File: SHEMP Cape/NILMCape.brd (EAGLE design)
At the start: 54.6 x 71.8 mm, 26 parts, among them U1 ADS8568_PM_64, U2 ACS756KCA-050B-PFF-T, U3 LTC6082, U4 LTC6082, U5 LM2687_DGK_8

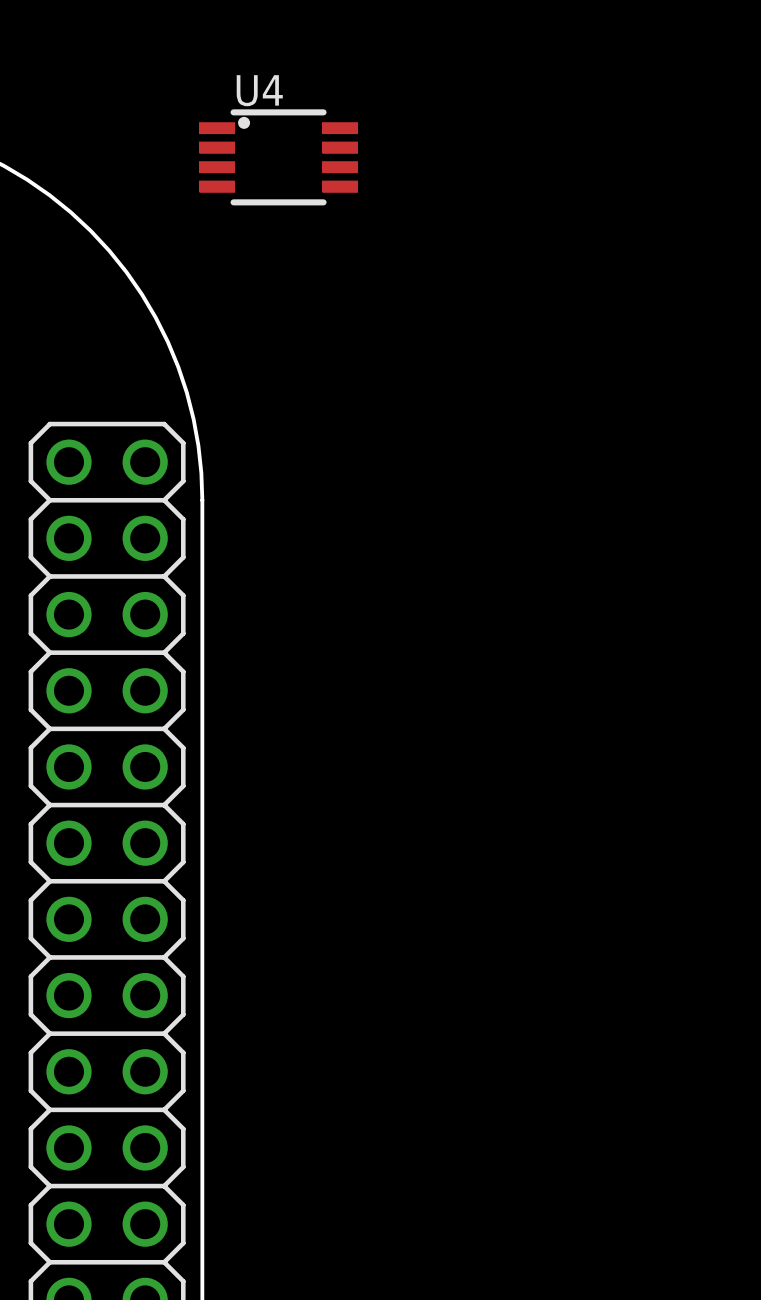
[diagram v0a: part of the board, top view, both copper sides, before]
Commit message: Added Frequency Response
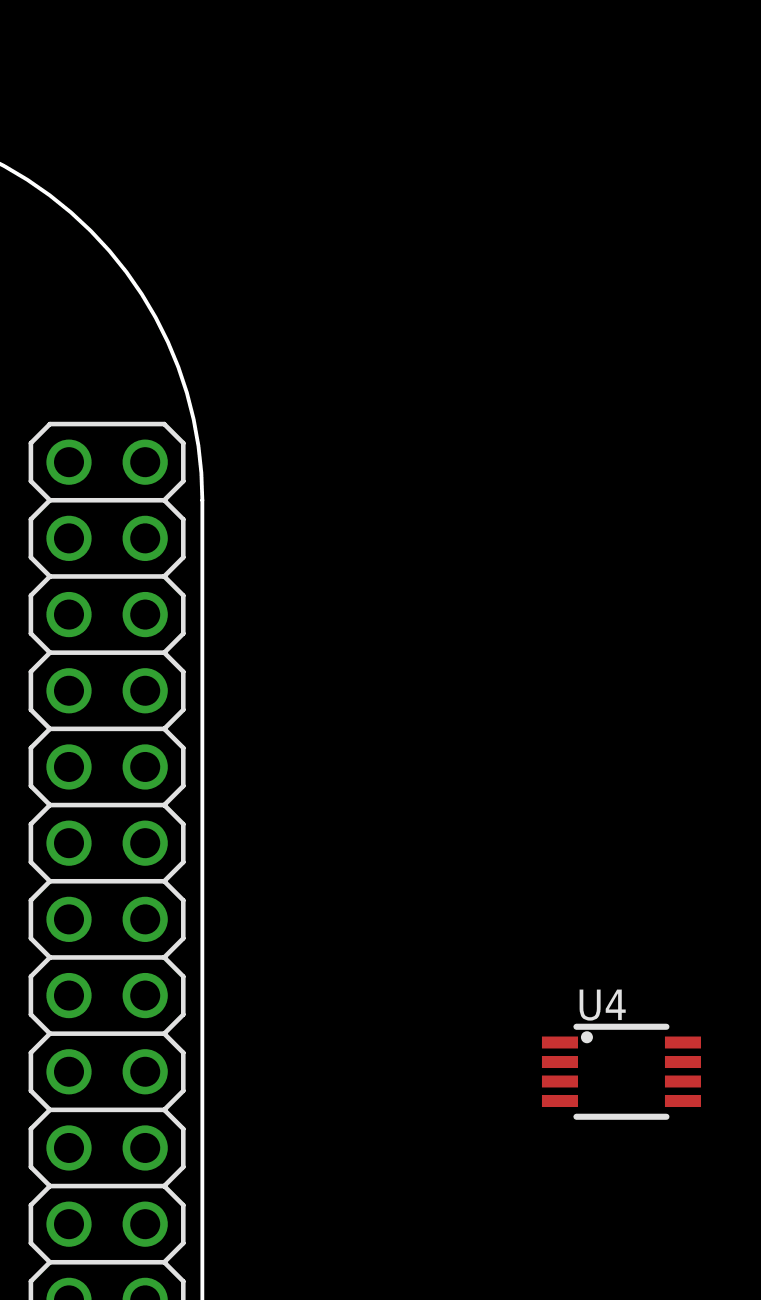
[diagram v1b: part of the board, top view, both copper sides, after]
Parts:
- moved U4 32.6 mm to (68.6, 54.6)
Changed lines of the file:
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@@
 <?xml version="1.0" encoding="utf-8"?>
 <!DOCTYPE eagle SYSTEM "eagle.dtd">
-<eagle version="6.4">
+<eagle version="6.5.0">
 <drawing>
 <settings>
@@
 <attribute name="VALUE" x="19.97" y="87.71" size="1.27" layer="27" font="vector"/>
 </element>
-<element name="U4" library="SensorCape" package="MSOP8" value="LTC6082" x="57.15" y="85.09" smashed="yes" rot="R270">
-<attribute name="NAME" x="55.646" y="86.814" size="1.016" layer="25"/>
-<attribute name="VALUE" x="55.538" y="82.262" size="1.016" layer="27"/>
+<element name="U4" library="SensorCape" package="MSOP8" value="LTC6082" x="68.58" y="54.61" smashed="yes" rot="R270">
+<attribute name="NAME" x="67.076" y="56.334" size="1.016" layer="25"/>
+<attribute name="VALUE" x="66.968" y="51.782" size="1.016" layer="27"/>
 </element>
 <element name="R1" library="SensorCape" package="0805" value="100k" x="29.21" y="53.975" smashed="yes">
@@
 <contactref element="U3" pad="8"/>
 <contactref element="U4" pad="8"/>
-<wire x1="38.88" y1="55.585" x2="59.2" y2="86.065" width="0" layer="19" extent="1-1"/>
+<wire x1="38.88" y1="55.585" x2="70.63" y2="55.585" width="0" layer="19" extent="1-1"/>
 </signal>
 <signal name="V-">
 <contactref element="U3" pad="4"/>
 <contactref element="U4" pad="4"/>
-<wire x1="34.78" y1="53.635" x2="55.1" y2="84.115" width="0" layer="19" extent="1-1"/>
+<wire x1="34.78" y1="53.635" x2="66.53" y2="53.635" width="0" layer="19" extent="1-1"/>
 </signal>
 <signal name="AVDD">

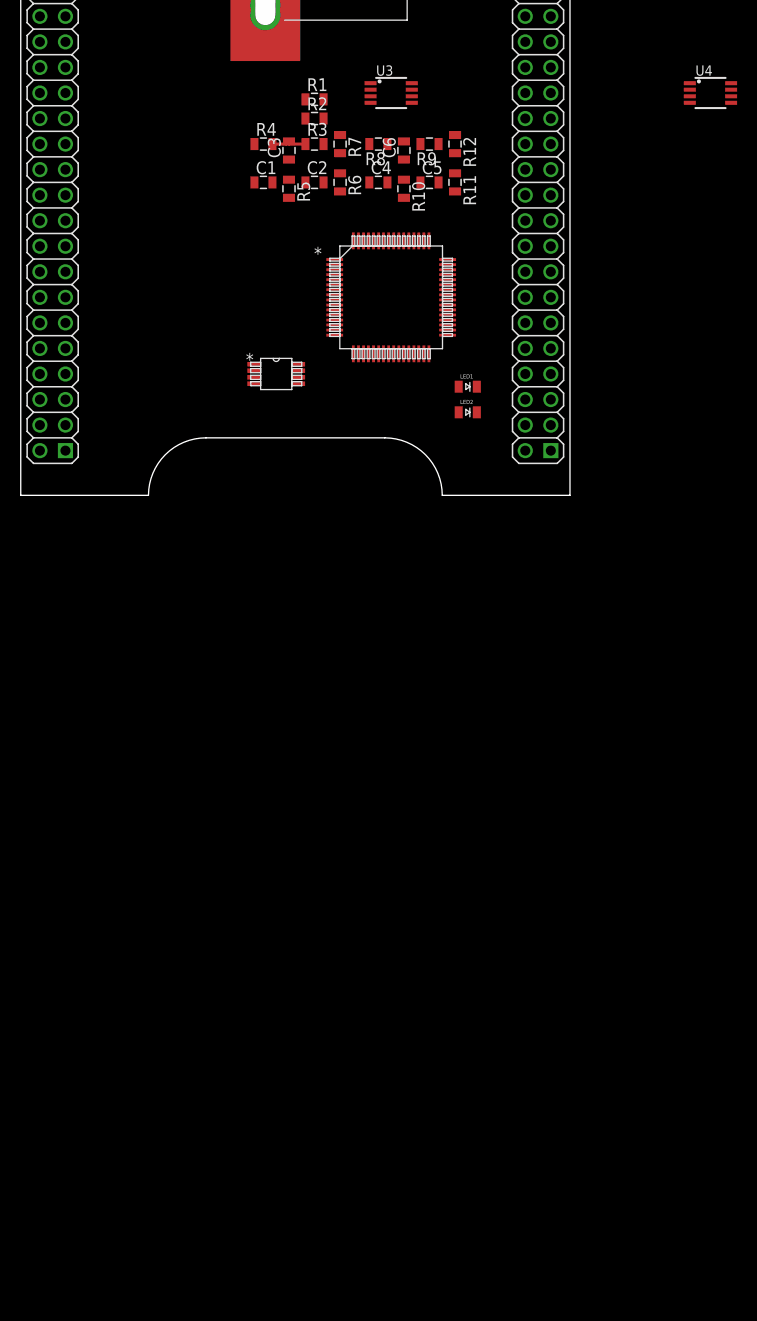
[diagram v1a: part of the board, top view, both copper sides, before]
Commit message: Split rail work, finished filtering stage.
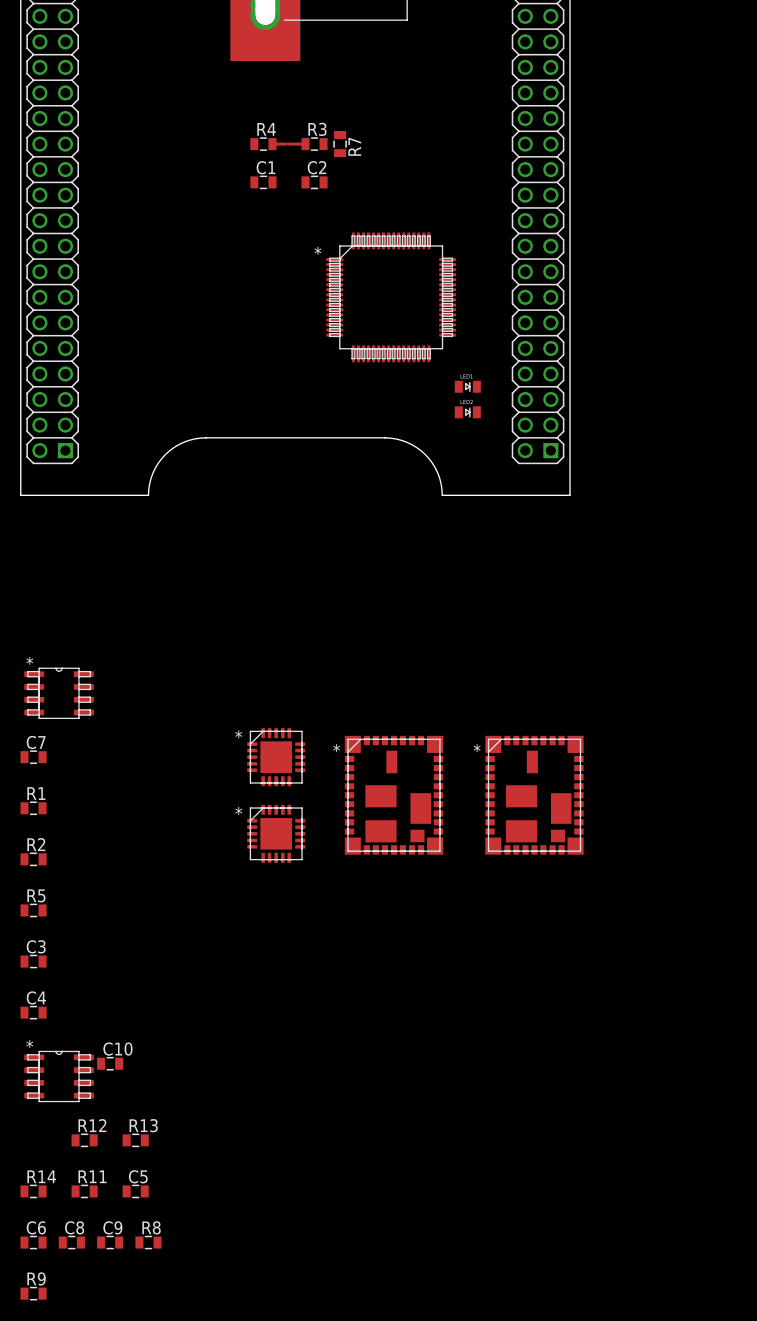
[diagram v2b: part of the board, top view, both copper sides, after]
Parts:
- removed R10: 4.1k, SensorCape:0805
- removed R6: 1k, SensorCape:0805
- added C10, C9: .33uF, SensorCape:0805
- added C7, C8: 1uF, SensorCape:0805
- added R13, R14: 8.2k, SensorCape:0805
- added U$2: TPS84259_RKG_41, SensorCape:RKG41
- added U$3: TPS7A4700_RGW_20, SensorCape:RGW20_3P15X3P15
- added U6: TPS7A3301_RGW_20, SensorCape:RGW20_3P15X3P15
- C3, C6: value .66uF -> .33uF
- R1: value 100k -> 1k
- R11: value 1k -> 15k
- R12: value 20k -> 1k
- R2: value 9.07k -> 8.2k
- R5: value 4.1k -> 8.2k
- R7: value 10k -> 1k
- U3, U4: value LTC6082 -> TLC2272A_D_8; device SensorCape:MSOP8 -> SensorCape:D8
- U5: value LM2687_DGK_8 -> TPS84250_RKG_41; device SensorCape:MUA08A -> SensorCape:RKG41
- moved R9 120.9 mm to (1.27, -64.8), turned to 0 degrees
- moved U4 117.3 mm to (3.81, -43.2), turned to 0 degrees
- moved C6 114.7 mm to (1.27, -59.7), turned to 0 degrees
- moved R8 111.6 mm to (12.7, -59.7), turned to 0 degrees
- moved R11 106.9 mm to (6.35, -54.6), turned to 0 degrees
- moved R12 105.7 mm to (6.35, -49.5), turned to 0 degrees
- moved C5 104.5 mm to (11.4, -54.6)
- moved C4 89.4 mm to (1.27, -36.8)
- moved C3 84.6 mm to (1.27, -31.8), turned to 0 degrees
- moved R2 78.8 mm to (1.27, -21.6)
- moved R5 76.1 mm to (1.27, -26.7), turned to 0 degrees
- moved R1 75.8 mm to (1.27, -16.5)
- moved U3 68.2 mm to (3.81, -5.08), turned to 0 degrees
- moved U5 42.7 mm to (47.0, -10.2)
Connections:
- net DGND renamed GND
- net DVDD renamed VDD_3V3EXP
- removed net AVDD: U$1.53, U$1.54
- removed net N$1: R1.1
- removed net N$14: C6.2, R8.1, R9.2
- removed net N$5: C2.2, R4.1, R6.2
- removed net V+: U3.8, U4.8
- removed net V-: U3.4, U4.4
- new net N$17: C7.1, U3.1, U3.2
- new net N$30: C7.2, R1.2
- new net N$31: R1.1, R7.2, U3.6
- new net N$32: R11.2, R12.1, U4.6
- new net N$33: U4.7
- new net SYS_5V: U$1.53
- new net VDD_5V: U$1.51, U$1.52
- net AGND: now also C10.1, C4.1, C9.1, R13.2, R14.2, R2.2, U4.5; no longer R10.2, R2.1, U3.3
- net HVDD: now also U3.8, U4.8; no longer U$1.51, U$1.52
- net HVSS: now also U3.4, U4.4; no longer U5.7
- net N$10: now also C5.1, U3.7; no longer C4.1, R7.1, U3.1
- net N$11: now also C5.2, C6.1, R13.1, R14.1; no longer R11.1, R12.2, U3.6
- net N$13: now also C10.2, C9.2, R8.1, R9.2; no longer C4.2, C5.1, R10.1
- net N$15: now also C6.2, U4.3; no longer C5.2, R11.2
- net N$16: now also C8.1, U4.1, U4.2; no longer C6.1
- net N$18: now also C8.2, R12.2; no longer R12.1, U3.7
- net N$2: no longer R1.2, R2.2
- net N$3: now also R2.1
- net N$4: now also C4.2
- net N$9: now also C2.2, R4.1, U3.3; no longer R6.1, R7.2, U3.2
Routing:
- net N$4: track 3.65 -> 3.01 mm

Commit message: More schematic capture work.
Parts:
- removed U3, U4: TLC2272A_D_8, SensorCape:D8
- added C11: 1uF, SensorCape:0805
- added C12: 4.7uF 50V, SensorCape:1210
- added C13: 2.2uF 100V, SensorCape:1210
- added C14: 22uF 100V, ASL:CPOL-RADIAL-100UF-25V
- added C15, C16, C17, C18: 22uF 25V, SensorCape:1210
- added R10, R6: 1k, SensorCape:0805
- added R15: 174k, ASL:0805
- added R16: 63.4k, ASL:0805
- added U7: LP2950-33_KVU_3, SensorCape:KVU3
- added U9: TL074_PW_14, SensorCape:PW14
- C10: value .33uF -> 1uF
- C7: value 1uF -> .33uF
- C8: value 1uF -> 4.7uF 50V; device SensorCape:0805 -> SensorCape:1210
- R1, R7: value 1k -> 8.2k
- R11: value 15k -> 178k; device SensorCape:0805 -> ASL:0805
- R12: value 1k -> 0; device SensorCape:0805 -> ASL:0805
- R13, R14: value 8.2k -> 1k
- moved R5 185.6 mm to (58.4, 149.9)
- moved C3 185.6 mm to (58.4, 144.8)
- moved R2 185.6 mm to (58.4, 154.9)
- moved C4 135.2 mm to (59.7, 85.1), turned to 180 degrees
- moved U5 122.8 mm to (24.1, 110.5)
- moved U$2 122.3 mm to (12.7, 110.5)
- moved U6 120.9 mm to (6.35, 108.0)
- moved U$3 119.6 mm to (6.35, 99.1)
- moved R7 102.4 mm to (-8.89, -44.5), turned to 0 degrees
- moved U2 80.1 mm to (118.1, 104.1), turned to 270 degrees
- moved R12 59.1 mm to (-21.6, -101.6)
- moved R11 50.4 mm to (-21.6, -96.5)
- moved C5 31.5 mm to (-12.7, -34.3)
- moved R1 31.2 mm to (-12.7, -44.5)
- moved C7 31.2 mm to (-12.7, -39.4)
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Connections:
- net N$2 renamed HOT_IN
- removed net N$15: C6.2, R9.1, U4.3
- removed net N$16: C8.1, U4.1, U4.2
- removed net N$32: R11.2, R12.1, U4.6
- removed net N$33: U4.7
- new net HVSS_15D: C15.2, C16.2, C17.2, C18.2, U$2.16, U$2.17, U$2.18, U$2.19, U$2.20, U$2.40
- new net N$1: C5.1, R1.2, R6.2, U9.7
- new net N$14: C10.2, U9.8, U9.9
- new net N$34: C11.2, R10.2
- new net N$35: C11.1, U9.1, U9.2
- new net N$36: R15.1, R16.2, U$2.27
- new net N$37: R12.1, R16.1, U$2.1, U$2.32, U$2.33, U$2.34, U$2.37, U$2.4, U$2.5
- new net N$5: R10.1, R6.1, U9.6
- new net SIGNAL_TO_AA: R14.1, U9.14
- new net VIN: C12.1, C13.1, C14.1, C8.1, R15.2, U$2.26
- net AGND: now also C7.1, R8.2, R9.2, U9.12, U9.5; no longer C10.1, R13.2, R14.2, U3.5, U4.5
- net GND: now also C12.2, C13.2, C14.2, C15.1, C16.1, C17.1, C18.1, C8.2, R11.2, U$2.10, U$2.11, U$2.12, U$2.13, U$2.14, U$2.15, U$2.39
- net HVDD: now also U9.4; no longer U3.8, U4.8
- net HVSS: now also U9.11; no longer U3.4, U4.4
- net N$10: now also C5.2, C6.1, R8.1, R9.1; no longer C5.1, R8.2, U3.7
- net N$11: now also C7.2, C9.2, R1.1, R7.2; no longer C5.2, C6.1, R13.1, R14.1
- net N$13: now also C6.2, R7.1, U9.10; no longer C10.2, C9.2, R8.1, R9.2
- net N$17: now also R13.2, R14.2, U9.13; no longer C7.1, U3.1, U3.2
- net N$18: now also R11.1, U$2.36; no longer C8.2, R12.2
- net N$30: now also C10.1, R13.1; no longer C7.2, R1.2
- net N$31: now also R12.2, U$2.30; no longer R1.1, R7.2, U3.6
- net N$9: now also U9.3; no longer U3.3
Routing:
- net N$4: track 3.01 -> 0.00 mm
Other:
- board size 54.6 x 71.8 mm -> 100 x 100 mm

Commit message: More schematic capture work.
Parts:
- added C19, C26, C31: 10nF, SensorCape:0805
- added C20, C23, C25: 22uF, SensorCape:1210
- added C21, C22, C24: 2.2uF 100V, SensorCape:1210
- added C27: 27uF 100V, SensorCape:CPOL-RADIAL-100UF-25V
- added C28, C30: 1uF, SensorCape:0805
- added C29, C32: 47uF, SensorCape:1210
- added C33: 10uF, SensorCape:CPOL-RADIAL-10UF-25V
- added C34, C35, C36, C37, C38, C39, C40, C41, C42, C43, C44, C45: .1uF, SensorCape:0805
- added R17, R18: 178k, ASL:0805
- added R19: 174k, ASL:0805
- added R20: 15.8k, ASL:0805
- added R21, R22: 0, ASL:0805
- added R23: 1.5M, ASL:0805
- added R24: 162k, ASL:0805
- added U10, U11, U12, U13, U3, U8: SI8663BC-B-IS1, SensorCape:SOIC-16
- added U14, U4: SN74CBT16390_DGG, SensorCape:DGG56
- R16: value 63.4k -> 15.8k
- moved C14 263.3 mm to (158.8, 120.7)
- moved C15 263.3 mm to (158.8, 113.0)
- moved C16 263.3 mm to (158.8, 109.2)
- moved C17 263.3 mm to (158.8, 105.4)
- moved C18 263.3 mm to (158.8, 101.6)
- moved R11 263.3 mm to (157.5, 96.5)
- moved R12 263.3 mm to (157.5, 91.4)
- moved R15 263.3 mm to (157.5, 86.4)
- moved R16 263.3 mm to (157.5, 81.3)
- moved C10 219.6 mm to (73.7, 147.3)
- moved C11 219.6 mm to (73.7, 177.8)
- moved C12 219.6 mm to (73.7, 129.5)
- moved C13 219.6 mm to (73.7, 125.7)
- moved C7 219.6 mm to (73.7, 162.6)
- moved C8 219.6 mm to (73.7, 133.3)
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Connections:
- new net ADC_DB0: U1.33, U14.1
- new net ADC_DB1: U1.32, U14.54
- new net ADC_DB10: U1.21, U14.18
- new net ADC_DB11: U1.20, U14.37
- new net ADC_DB12: U1.19, U14.21
- new net ADC_DB13: U1.18, U14.34
- new net ADC_DB14: U1.17, U14.24
- new net ADC_DB15: U1.16, U14.31
- new net ADC_DB2: U1.31, U14.4
- new net ADC_DB3: U1.30, U14.51
- new net ADC_DB4: U1.29, U14.7
- new net ADC_DB5: U1.28, U14.48
- new net ADC_DB6: U1.27, U14.10
- new net ADC_DB7: U1.26, U14.45
- new net ADC_DB8: U1.23, U14.15
- new net ADC_DB9: U1.22, U14.40
- new net BB_DB0: U4.1
- new net BB_DB1: U4.54
- new net BB_DB10: U4.18
- new net BB_DB11: U4.37
- new net BB_DB12: U4.21
- new net BB_DB13: U4.34
- new net BB_DB14: U4.24
- new net BB_DB15: U4.31
- new net BB_DB2: U4.4
- new net BB_DB3: U4.51
- new net BB_DB4: U4.7
- new net BB_DB5: U4.48
- new net BB_DB6: U4.10
- new net BB_DB7: U4.45
- new net BB_DB8: U4.15
- new net BB_DB9: U4.40
- new net HVDD_12A: C29.1, U$3.1, U$3.20, U$3.3
- new net HVDD_15D: C20.2, C23.2, C25.2, R17.2, U$3.13, U$3.15, U$3.16, U5.10, U5.11, U5.12, U5.13, U5.14, U5.15, U5.39, U7.3
- new net HVSS_12A: C31.1, C32.1, R23.2, U6.1, U6.20
- new net N$100: U$1.77
- new net N$15: C19.1, U$2.28
- new net N$16: C31.2, R24.2, U6.3
- new net N$2: C20.1, C21.2, C22.2, C23.1, C24.2, C25.1, C27.2, R21.2, U5.1, U5.16, U5.17, U5.18, U5.19, U5.20, U5.30, U5.32, U5.33, U5.34, U5.37, U5.4, U5.40, U5.5
- new net N$32: C12.2, C13.2, C14.2, C15.1, C16.1, C17.1, C18.1, C8.2, R11.2, R22.2, U$2.10, U$2.11, U$2.12, U$2.13, U$2.14, U$2.15, U$2.39
- new net N$33: C30.1, U6.14
- new net N$38: R18.2, U5.31
- new net N$39: U$1.27
- new net N$40: U$1.29
- new net N$41: R19.1, R20.2, U5.27
- new net N$42: U$1.28
- new net N$43: C26.1, U5.28
- new net N$44: C26.2, R18.1, R20.1, R21.1, U5.29, U5.8, U5.9
- new net N$45: C28.1, U$3.14
- new net N$46: U$1.30
- new net N$47: U$1.31
- new net N$48: U$1.33
- new net N$49: U$1.35
- new net N$50: U$1.37
- new net N$51: U$1.32
- new net N$52: U$1.34
- new net N$53: U$1.36
- new net N$54: U$1.38
- new net N$55: U$1.45
- new net N$56: U$1.46
- new net N$57: U$1.43
- new net N$58: U$1.44
- new net N$59: U$1.41
- new net N$60: U$1.42
- new net N$61: U$1.39
- new net N$62: U$1.40
- new net N$63: U$1.11
- new net N$64: U$1.12
- new net N$65: C44.1
- new net N$66: C34.1
- new net N$67: U$1.13
- new net N$68: U$1.14
- new net N$69: U$1.15
- new net N$70: U$1.16
- new net N$71: U$1.17
- new net N$72: U$1.19
- new net N$73: U$1.20
- new net N$74: U$1.21
- new net N$75: U$1.18
- new net N$76: U$1.22
- new net N$77: U$1.7
- new net N$78: U$1.3
- new net N$79: U$1.5
- new net N$80: U$1.4
- new net N$81: U$1.6
- new net N$82: U$1.24
- new net N$83: U$1.26
- new net N$84: U$1.23
- new net N$85: U$1.25
- new net N$86: U$1.58
- new net N$87: U$1.73
- new net N$88: U$1.71
- new net N$89: U$1.69
- new net N$90: U$1.9
- new net N$91: U$1.8
- new net N$92: U$1.10
- new net N$93: U$1.61
- new net N$94: U$1.88
- new net N$95: U$1.67
- new net N$96: U$1.68
- new net N$97: U$1.57
- new net N$98: U$1.59
- new net N$99: U$1.75
- new net R_DB0: U12.15, U4.56
- new net R_DB1: U12.14, U4.55
- new net R_DB10: U3.14, U4.39
- new net R_DB11: U3.13, U4.38
- new net R_DB12: U4.36, U8.15
- new net R_DB13: U4.35, U8.14
- new net R_DB14: U4.33, U8.13
- new net R_DB15: U13.15, U4.32
- new net R_DB2: U12.13, U4.53
- new net R_DB3: U11.15, U4.52
- new net R_DB4: U11.14, U4.50
- new net R_DB5: U11.13, U4.49
- new net R_DB6: U10.15, U4.47
- new net R_DB7: U10.14, U4.46
- new net R_DB8: U10.13, U4.42
- new net R_DB9: U3.15, U4.41
- new net R_DB_ADC0: U12.5, U14.56
- new net R_DB_ADC1: U12.6, U14.55
- new net R_DB_ADC10: U14.39, U3.6
- new net R_DB_ADC11: U14.38, U3.7
- new net R_DB_ADC12: U14.36, U8.5
- new net R_DB_ADC13: U14.35, U8.6
- new net R_DB_ADC14: U14.33, U8.7
- new net R_DB_ADC15: U13.5, U14.32
- new net R_DB_ADC2: U12.7, U14.53
- new net R_DB_ADC3: U11.5, U14.52
- new net R_DB_ADC4: U11.6, U14.50
- new net R_DB_ADC5: U11.7, U14.49
- new net R_DB_ADC6: U10.5, U14.47
- new net R_DB_ADC7: U10.6, U14.46
- new net R_DB_ADC8: U10.7, U14.42
- new net R_DB_ADC9: U14.41, U3.5
- new net VDD3V3_D: C33.1, C34.2, C35.2, C36.2, C37.2, C38.2, C39.2, C40.2, C41.2, C42.2, C43.2, C44.2, C45.2, U10.1, U10.16, U11.1, U11.16, U12.1, U12.16, U13.1, U13.16, U3.1, U3.16, U7.1, U8.1, U8.16
- new net W_DB0: U12.12, U4.2
- new net W_DB1: U12.11, U4.3
- new net W_DB10: U3.11, U4.19
- new net W_DB11: U3.10, U4.20
- new net W_DB12: U4.22, U8.12
- new net W_DB13: U4.23, U8.11
- new net W_DB14: U4.25, U8.10
- new net W_DB15: U13.12, U4.26
- new net W_DB2: U12.10, U4.5
- new net W_DB3: U11.12, U4.6
- new net W_DB4: U11.11, U4.8
- new net W_DB5: U11.10, U4.9
- new net W_DB6: U10.12, U4.11
- new net W_DB7: U10.11, U4.12
- new net W_DB8: U10.10, U4.16
- new net W_DB9: U3.12, U4.17
- new net W_DB_ADC0: U12.2, U14.2
- new net W_DB_ADC1: U12.3, U14.3
- new net W_DB_ADC10: U14.19, U3.3
- new net W_DB_ADC11: U14.20, U3.4
- new net W_DB_ADC12: U14.22, U8.2
- new net W_DB_ADC13: U14.23, U8.3
- new net W_DB_ADC14: U14.25, U8.4
- new net W_DB_ADC15: U13.2, U14.26
- new net W_DB_ADC2: U12.4, U14.5
- new net W_DB_ADC3: U11.2, U14.6
- new net W_DB_ADC4: U11.3, U14.8
- new net W_DB_ADC5: U14.9
- new net W_DB_ADC6: U10.2, U11.4, U14.11
- new net W_DB_ADC7: U10.3, U14.12
- new net W_DB_ADC8: U10.4, U14.16
- new net W_DB_ADC9: U14.17, U3.2
- net GND: now also C19.2, C28.2, C29.2, C30.2, C32.2, C33.2, C35.1, C36.1, C37.1, C38.1, C39.1, C40.1, C41.1, C42.1, C43.1, C45.1, R12.1, R16.1, R22.1, R24.1, U$2.1, U$2.32, U$2.33, U$2.34, U$2.37, U$2.4, U$2.5, U$2.8, U$2.9, U$3.11, U$3.21, U$3.4, U$3.6, U$3.7, U$3.9, U10.8, U10.9, U11.8, U11.9, U12.8, U12.9, U13.8, U13.9, U3.8, U3.9, U6.21, U6.7, U7.2, U8.8, U8.9; no longer C12.2, C13.2, C14.2, C15.1, C16.1, C17.1, C18.1, C8.2, R11.2, U$2.10, U$2.11, U$2.12, U$2.13, U$2.14, U$2.15, U$2.39
- net HVSS_15D: now also U6.13, U6.15, U6.16
- net N$37: now also R17.1, U5.36; no longer R12.1, R16.1, U$2.1, U$2.32, U$2.33, U$2.34, U$2.37, U$2.4, U$2.5
- net VIN: now also C21.1, C22.1, C24.1, C27.1, R19.2, U5.26
